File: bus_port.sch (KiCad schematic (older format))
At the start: 0 parts

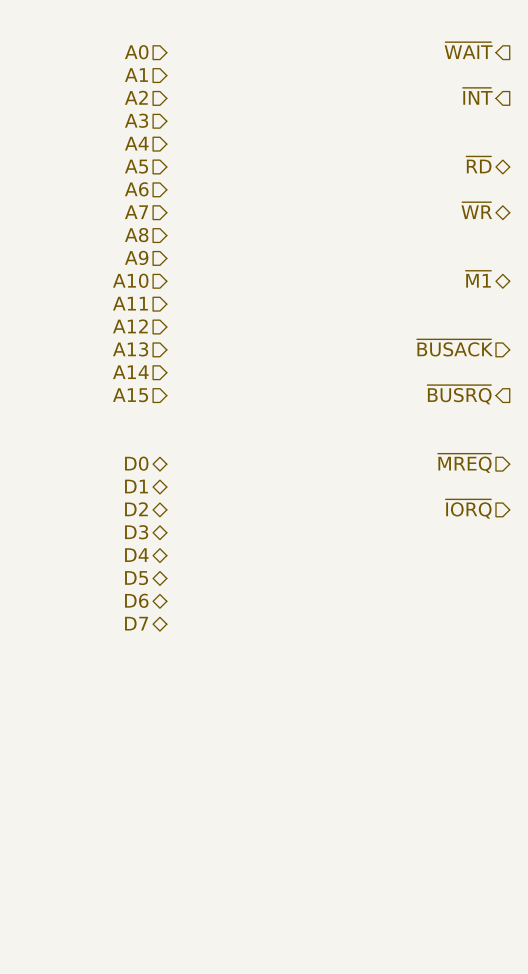
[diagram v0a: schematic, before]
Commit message: More WIP added hierarchical sheets for bus
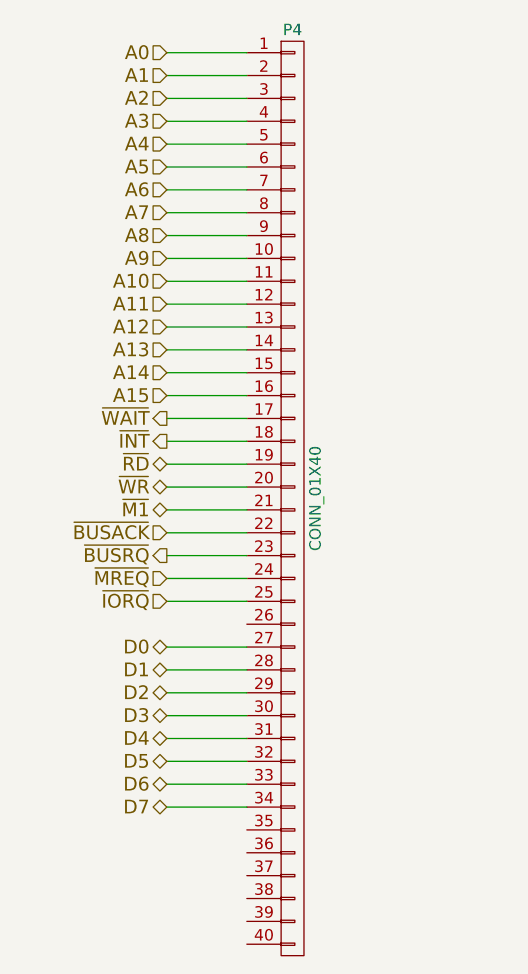
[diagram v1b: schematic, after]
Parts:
- added P1: CONN_01X40, Socket_Strips:Socket_Strip_Straight_1x40, symbol CONN_01X40
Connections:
- net A0: now also P1.1 (P1)
- net A1: now also P1.2 (P2)
- net A10: now also P1.11 (P11)
- net A11: now also P1.12 (P12)
- net A12: now also P1.13 (P13)
- net A13: now also P1.14 (P14)
- net A14: now also P1.15 (P15)
- net A15: now also P1.16 (P16)
- net A2: now also P1.3 (P3)
- net A3: now also P1.4 (P4)
- net A4: now also P1.5 (P5)
- net A5: now also P1.6 (P6)
- net A6: now also P1.7 (P7)
- net A7: now also P1.8 (P8)
- net A8: now also P1.9 (P9)
- net A9: now also P1.10 (P10)
- net D0: now also P1.27 (P27)
- net D1: now also P1.28 (P28)
- net D2: now also P1.29 (P29)
- net D3: now also P1.30 (P30)
- net D4: now also P1.31 (P31)
- net D5: now also P1.32 (P32)
- net D6: now also P1.33 (P33)
- net D7: now also P1.34 (P34)
- net ~BUSACK: now also P1.22 (P22)
- net ~BUSRQ: now also P1.23 (P23)
- net ~INT: now also P1.18 (P18)
- net ~IORQ: now also P1.25 (P25)
- net ~M1: now also P1.21 (P21)
- net ~MREQ: now also P1.24 (P24)
- net ~RD: now also P1.19 (P19)
- net ~WAIT: now also P1.17 (P17)
- net ~WR: now also P1.20 (P20)
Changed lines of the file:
@@
 $Descr A4 11693 8268
 encoding utf-8
-Sheet 4 4
+Sheet 7 7
 Title ""
 Date ""
@@
 Text HLabel 1500 3000 0    60   Input ~ 0
 A15
+Text HLabel 1500 4100 0    60   3State ~ 0
+D0
+Text HLabel 1500 4200 0    60   3State ~ 0
+D1
+Text HLabel 1500 4300 0    60   3State ~ 0
+D2
+Text HLabel 1500 4400 0    60   3State ~ 0
+D3
+Text HLabel 1500 4500 0    60   3State ~ 0
+D4
+Text HLabel 1500 4600 0    60   3State ~ 0
+D5
+Text HLabel 1500 4700 0    60   3State ~ 0
+D6
+Text HLabel 1500 4800 0    60   3State ~ 0
+D7
+Text HLabel 1500 3100 0    60   Output ~ 0
+~WAIT
+Text HLabel 1500 3200 0    60   Output ~ 0
+~INT
 Text HLabel 1500 3300 0    60   3State ~ 0
-D0
+~RD
 Text HLabel 1500 3400 0    60   3State ~ 0
-D1
+~WR
 Text HLabel 1500 3500 0    60   3State ~ 0
-D2
-Text HLabel 1500 3600 0    60   3State ~ 0
-D3
-Text HLabel 1500 3700 0    60   3State ~ 0
-D4
-Text HLabel 1500 3800 0    60   3State ~ 0
-D5
-Text HLabel 1500 3900 0    60   3State ~ 0
-D6
-Text HLabel 1500 4000 0    60   3State ~ 0
-D7
-Text HLabel 3000 1500 0    60   Output ~ 0
-~WAIT
-Text HLabel 3000 1700 0    60   Output ~ 0
-~INT
-Text HLabel 3000 2000 0    60   3State ~ 0
-~RD
-Text HLabel 3000 2200 0    60   3State ~ 0
-~WR
-Text HLabel 3000 2500 0    60   3State ~ 0
 ~M1
-Text HLabel 3000 2800 0    60   Input ~ 0
+Text HLabel 1500 3600 0    60   Input ~ 0
 ~BUSACK
-Text HLabel 3000 3000 0    60   Output ~ 0
+Text HLabel 1500 3700 0    60   Output ~ 0
 ~BUSRQ
-Text HLabel 3000 3300 0    60   Input ~ 0
+Text HLabel 1500 3800 0    60   Input ~ 0
 ~MREQ
-Text HLabel 3000 3500 0    60   Input ~ 0
+Text HLabel 1500 3900 0    60   Input ~ 0
 ~IORQ
+$Comp
+L CONN_01X40 P1
+U 1 1 577CEB68
+P 2050 3450
+AR Path="/577BB11C/577CEB68" Ref="P1"  Part="1"
+AR Path="/577C4BD1/577CEB68" Ref="P2"  Part="1"
+AR Path="/577F17CE/577F1897/577CEB68" Ref="P1"  Part="1"
+AR Path="/577F17CE/577F7EB3/577CEB68" Ref="P2"  Part="1"
+AR Path="/577F17CE/577F8AF5/577CEB68" Ref="P3"  Part="1"
+AR Path="/577F17CE/577F9440/577CEB68" Ref="P4"  Part="1"
+F 0 "P4" H 2050 5500 50  0000 C CNN
+F 1 "CONN_01X40" V 2150 3450 50  0000 C CNN
+F 2 "Socket_Strips:Socket_Strip_Straight_1x40" H 2050 3450 50  0001 C CNN
+F 3 "" H 2050 3450 50  0000 C CNN
+	1    2050 3450
+	1    0    0    -1
+$EndComp
+Wire Wire Line
+	1500 1500 1850 1500
+Wire Wire Line
+	1500 1600 1850 1600
+Wire Wire Line
+	1500 1700 1850 1700
+Wire Wire Line
+	1500 1800 1850 1800
+Wire Wire Line
+	1500 1900 1850 1900
+Wire Wire Line
+	1500 2000 1850 2000
+Wire Wire Line
+	1500 2100 1850 2100
+Wire Wire Line
+	1500 2200 1850 2200
+Wire Wire Line
+	1500 2300 1850 2300
+Wire Wire Line
+	1500 2400 1850 2400
+Wire Wire Line
+	1500 2500 1850 2500
+Wire Wire Line
+	1500 2600 1850 2600
+Wire Wire Line
+	1500 2700 1850 2700
+Wire Wire Line
+	1500 2800 1850 2800
+Wire Wire Line
+	1500 2900 1850 2900
+Wire Wire Line
+	1500 3000 1850 3000
+Wire Wire Line
+	1500 4100 1850 4100
+Wire Wire Line
+	1500 4200 1850 4200
+Wire Wire Line
+	1500 4300 1850 4300
+Wire Wire Line
+	1500 4400 1850 4400
+Wire Wire Line
+	1500 4500 1850 4500
+Wire Wire Line
+	1500 4600 1850 4600
+Wire Wire Line
+	1500 4700 1850 4700
+Wire Wire Line
+	1500 4800 1850 4800
+Wire Wire Line
+	1500 3100 1850 3100
+Wire Wire Line
+	1500 3200 1850 3200
+Wire Wire Line
+	1500 3300 1850 3300
+Wire Wire Line
+	1500 3400 1850 3400
+Wire Wire Line
+	1500 3500 1850 3500
+Wire Wire Line
+	1500 3600 1850 3600
+Wire Wire Line
+	1500 3700 1850 3700
+Wire Wire Line
+	1500 3800 1850 3800
+Wire Wire Line
+	1500 3900 1850 3900
 $EndSCHEMATC

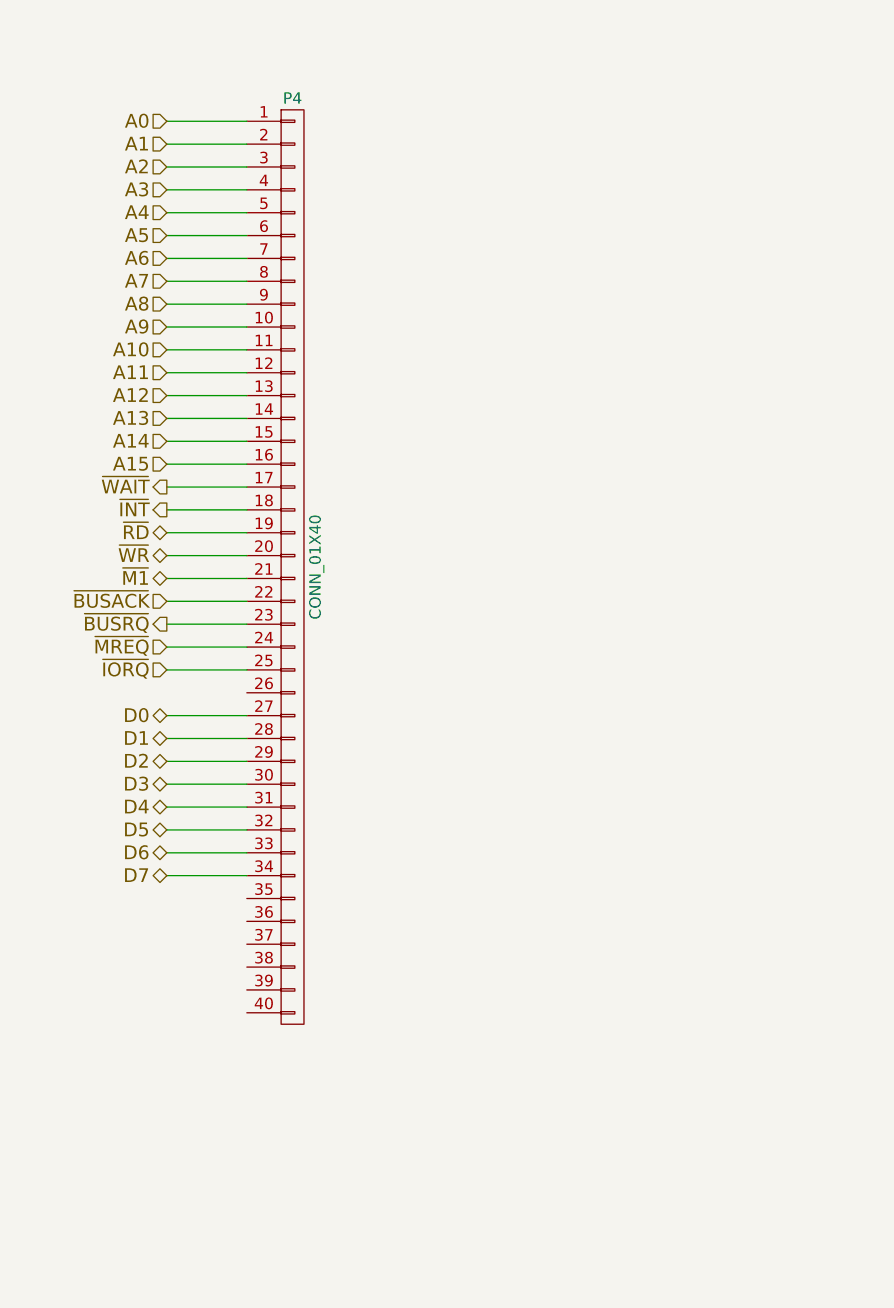
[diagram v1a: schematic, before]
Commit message: Added seperate power pin slots to stop inserting cards backwards
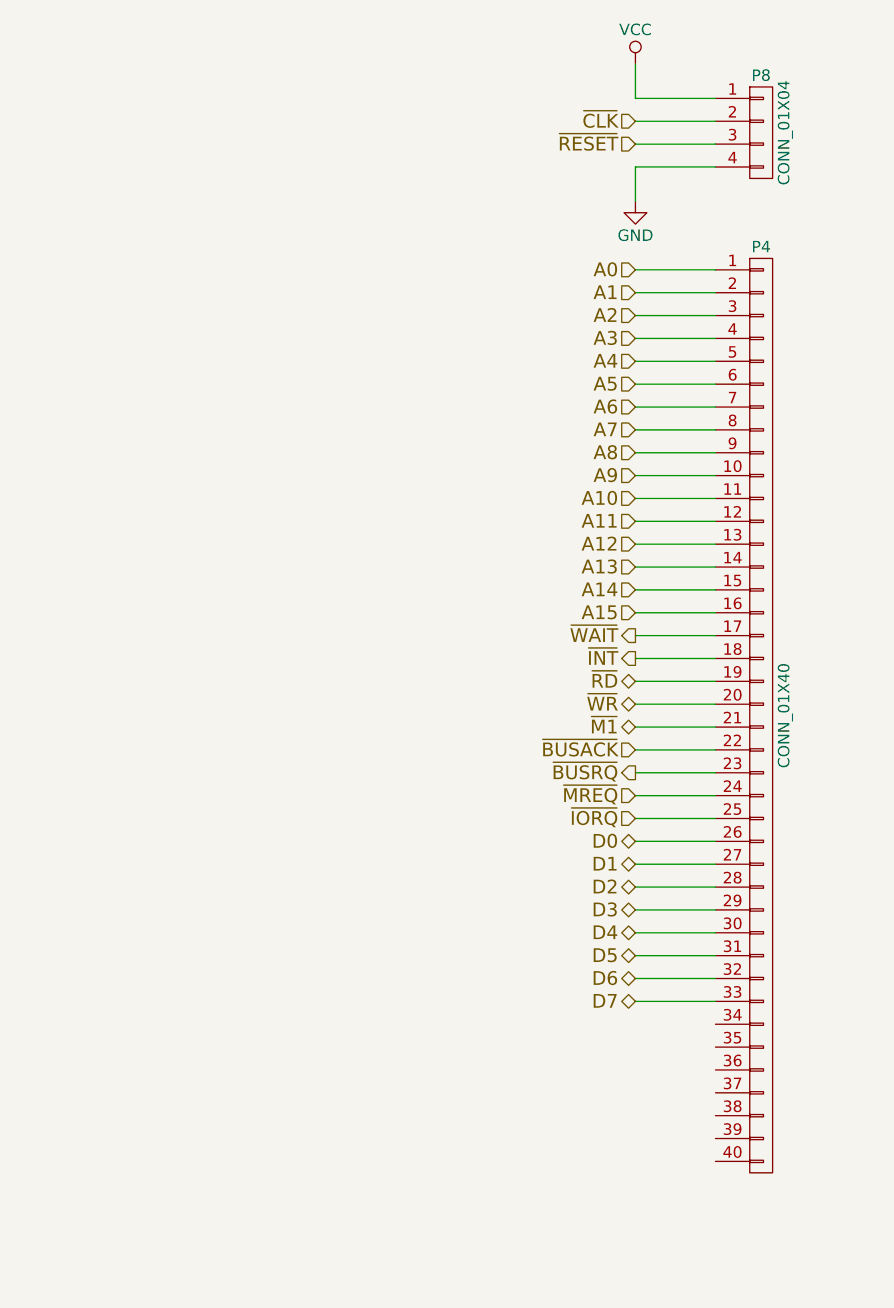
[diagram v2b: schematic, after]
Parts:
- added P5: CONN_01X04, symbol CONN_01X04
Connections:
- net D0: now also P1.26 (P26); no longer P1.27 (P27)
- net D1: now also P1.27 (P27); no longer P1.28 (P28)
- net D2: now also P1.28 (P28); no longer P1.29 (P29)
- net D3: now also P1.29 (P29); no longer P1.30 (P30)
- net D4: now also P1.30 (P30); no longer P1.31 (P31)
- net D5: now also P1.31 (P31); no longer P1.32 (P32)
- net D6: now also P1.32 (P32); no longer P1.33 (P33)
- net D7: now also P1.33 (P33); no longer P1.34 (P34)
- new net GND: P5.4 (P4)
- new net VCC: P5.1 (P1)
- new net ~CLK: P5.2 (P2)
- new net ~RESET: P5.3 (P3)
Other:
- moved on the sheet: P4
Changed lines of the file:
@@
 $Descr A4 11693 8268
 encoding utf-8
-Sheet 7 7
+Sheet 4 7
 Title ""
 Date ""
@@
 Comment4 ""
 $EndDescr
-Text HLabel 1500 1500 0    60   Input ~ 0
+Text HLabel 3550 2150 0    60   Input ~ 0
 A0
-Text HLabel 1500 1600 0    60   Input ~ 0
+Text HLabel 3550 2250 0    60   Input ~ 0
 A1
-Text HLabel 1500 1700 0    60   Input ~ 0
+Text HLabel 3550 2350 0    60   Input ~ 0
 A2
-Text HLabel 1500 1800 0    60   Input ~ 0
+Text HLabel 3550 2450 0    60   Input ~ 0
 A3
-Text HLabel 1500 1900 0    60   Input ~ 0
+Text HLabel 3550 2550 0    60   Input ~ 0
 A4
-Text HLabel 1500 2000 0    60   Input ~ 0
+Text HLabel 3550 2650 0    60   Input ~ 0
 A5
-Text HLabel 1500 2100 0    60   Input ~ 0
+Text HLabel 3550 2750 0    60   Input ~ 0
 A6
-Text HLabel 1500 2200 0    60   Input ~ 0
+Text HLabel 3550 2850 0    60   Input ~ 0
 A7
-Text HLabel 1500 2300 0    60   Input ~ 0
+Text HLabel 3550 2950 0    60   Input ~ 0
 A8
-Text HLabel 1500 2400 0    60   Input ~ 0
+Text HLabel 3550 3050 0    60   Input ~ 0
 A9
-Text HLabel 1500 2500 0    60   Input ~ 0
+Text HLabel 3550 3150 0    60   Input ~ 0
 A10
-Text HLabel 1500 2600 0    60   Input ~ 0
+Text HLabel 3550 3250 0    60   Input ~ 0
 A11
-Text HLabel 1500 2700 0    60   Input ~ 0
+Text HLabel 3550 3350 0    60   Input ~ 0
 A12
-Text HLabel 1500 2800 0    60   Input ~ 0
+Text HLabel 3550 3450 0    60   Input ~ 0
 A13
-Text HLabel 1500 2900 0    60   Input ~ 0
+Text HLabel 3550 3550 0    60   Input ~ 0
 A14
-Text HLabel 1500 3000 0    60   Input ~ 0
+Text HLabel 3550 3650 0    60   Input ~ 0
 A15
-Text HLabel 1500 4100 0    60   3State ~ 0
+Text HLabel 3550 4650 0    60   3State ~ 0
 D0
-Text HLabel 1500 4200 0    60   3State ~ 0
+Text HLabel 3550 4750 0    60   3State ~ 0
 D1
-Text HLabel 1500 4300 0    60   3State ~ 0
+Text HLabel 3550 4850 0    60   3State ~ 0
 D2
-Text HLabel 1500 4400 0    60   3State ~ 0
+Text HLabel 3550 4950 0    60   3State ~ 0
 D3
-Text HLabel 1500 4500 0    60   3State ~ 0
+Text HLabel 3550 5050 0    60   3State ~ 0
 D4
-Text HLabel 1500 4600 0    60   3State ~ 0
+Text HLabel 3550 5150 0    60   3State ~ 0
 D5
-Text HLabel 1500 4700 0    60   3State ~ 0
+Text HLabel 3550 5250 0    60   3State ~ 0
 D6
-Text HLabel 1500 4800 0    60   3State ~ 0
+Text HLabel 3550 5350 0    60   3State ~ 0
 D7
-Text HLabel 1500 3100 0    60   Output ~ 0
+Text HLabel 3550 3750 0    60   Output ~ 0
 ~WAIT
-Text HLabel 1500 3200 0    60   Output ~ 0
+Text HLabel 3550 3850 0    60   Output ~ 0
 ~INT
-Text HLabel 1500 3300 0    60   3State ~ 0
+Text HLabel 3550 3950 0    60   3State ~ 0
 ~RD
-Text HLabel 1500 3400 0    60   3State ~ 0
+Text HLabel 3550 4050 0    60   3State ~ 0
 ~WR
-Text HLabel 1500 3500 0    60   3State ~ 0
+Text HLabel 3550 4150 0    60   3State ~ 0
 ~M1
-Text HLabel 1500 3600 0    60   Input ~ 0
+Text HLabel 3550 4250 0    60   Input ~ 0
 ~BUSACK
-Text HLabel 1500 3700 0    60   Output ~ 0
+Text HLabel 3550 4350 0    60   Output ~ 0
 ~BUSRQ
-Text HLabel 1500 3800 0    60   Input ~ 0
+Text HLabel 3550 4450 0    60   Input ~ 0
 ~MREQ
-Text HLabel 1500 3900 0    60   Input ~ 0
+Text HLabel 3550 4550 0    60   Input ~ 0
 ~IORQ
 $Comp
 L CONN_01X40 P1
 U 1 1 577CEB68
-P 2050 3450
+P 4100 4100
 AR Path="/577BB11C/577CEB68" Ref="P1"  Part="1"
 AR Path="/577C4BD1/577CEB68" Ref="P2"  Part="1"
@@
 AR Path="/577F17CE/577F8AF5/577CEB68" Ref="P3"  Part="1"
 AR Path="/577F17CE/577F9440/577CEB68" Ref="P4"  Part="1"
-F 0 "P4" H 2050 5500 50  0000 C CNN
-F 1 "CONN_01X40" V 2150 3450 50  0000 C CNN
-F 2 "Socket_Strips:Socket_Strip_Straight_1x40" H 2050 3450 50  0001 C CNN
-F 3 "" H 2050 3450 50  0000 C CNN
-	1    2050 3450
-	1    0    0    -1
-$EndComp
-Wire Wire Line
-	1500 1500 1850 1500
-Wire Wire Line
-	1500 1600 1850 1600
-Wire Wire Line
-	1500 1700 1850 1700
-Wire Wire Line
-	1500 1800 1850 1800
-Wire Wire Line
-	1500 1900 1850 1900
-Wire Wire Line
-	1500 2000 1850 2000
-Wire Wire Line
-	1500 2100 1850 2100
-Wire Wire Line
-	1500 2200 1850 2200
-Wire Wire Line
-	1500 2300 1850 2300
-Wire Wire Line
-	1500 2400 1850 2400
-Wire Wire Line
-	1500 2500 1850 2500
-Wire Wire Line
-	1500 2600 1850 2600
-Wire Wire Line
-	1500 2700 1850 2700
-Wire Wire Line
-	1500 2800 1850 2800
-Wire Wire Line
-	1500 2900 1850 2900
-Wire Wire Line
-	1500 3000 1850 3000
-Wire Wire Line
-	1500 4100 1850 4100
-Wire Wire Line
-	1500 4200 1850 4200
-Wire Wire Line
-	1500 4300 1850 4300
-Wire Wire Line
-	1500 4400 1850 4400
-Wire Wire Line
-	1500 4500 1850 4500
-Wire Wire Line
-	1500 4600 1850 4600
-Wire Wire Line
-	1500 4700 1850 4700
-Wire Wire Line
-	1500 4800 1850 4800
-Wire Wire Line
-	1500 3100 1850 3100
-Wire Wire Line
-	1500 3200 1850 3200
-Wire Wire Line
-	1500 3300 1850 3300
-Wire Wire Line
-	1500 3400 1850 3400
-Wire Wire Line
-	1500 3500 1850 3500
-Wire Wire Line
-	1500 3600 1850 3600
-Wire Wire Line
-	1500 3700 1850 3700
-Wire Wire Line
-	1500 3800 1850 3800
-Wire Wire Line
-	1500 3900 1850 3900
+F 0 "P4" H 4100 6150 50  0000 C CNN
+F 1 "CONN_01X40" V 4200 4100 50  0000 C CNN
+F 2 "Socket_Strips:Socket_Strip_Straight_1x40" H 4100 4100 50  0001 C CNN
+F 3 "" H 4100 4100 50  0000 C CNN
+	1    4100 4100
+	1    0    0    -1
+$EndComp
+Wire Wire Line
+	3550 2150 3900 2150
+Wire Wire Line
+	3550 2250 3900 2250
+Wire Wire Line
+	3550 2350 3900 2350
+Wire Wire Line
+	3550 2450 3900 2450
+Wire Wire Line
+	3550 2550 3900 2550
+Wire Wire Line
+	3550 2650 3900 2650
+Wire Wire Line
+	3550 2750 3900 2750
+Wire Wire Line
+	3550 2850 3900 2850
+Wire Wire Line
+	3550 2950 3900 2950
+Wire Wire Line
+	3550 3050 3900 3050
+Wire Wire Line
+	3550 3150 3900 3150
+Wire Wire Line
+	3550 3250 3900 3250
+Wire Wire Line
+	3550 3350 3900 3350
+Wire Wire Line
+	3550 3450 3900 3450
+Wire Wire Line
+	3550 3550 3900 3550
+Wire Wire Line
+	3550 3650 3900 3650
+Wire Wire Line
+	3550 4650 3900 4650
+Wire Wire Line
+	3550 4750 3900 4750
+Wire Wire Line
+	3550 4850 3900 4850
+Wire Wire Line
+	3550 4950 3900 4950
+Wire Wire Line
+	3550 5050 3900 5050
+Wire Wire Line
+	3550 5150 3900 5150
+Wire Wire Line
+	3550 5250 3900 5250
+Wire Wire Line
+	3550 5350 3900 5350
+Wire Wire Line
+	3550 3750 3900 3750
+Wire Wire Line
+	3550 3850 3900 3850
+Wire Wire Line
+	3550 3950 3900 3950
+Wire Wire Line
+	3550 4050 3900 4050
+Wire Wire Line
+	3550 4150 3900 4150
+Wire Wire Line
+	3550 4250 3900 4250
+Wire Wire Line
+	3550 4350 3900 4350
+Wire Wire Line
+	3550 4450 3900 4450
+Wire Wire Line
+	3550 4550 3900 4550
+Text HLabel 3550 1500 0    60   Input ~ 0
+~CLK
+$Comp
+L CONN_01X04 P5
+U 1 1 578144F7
+P 4100 1550
+AR Path="/577F17CE/577F1897/578144F7" Ref="P5"  Part="1"
+AR Path="/577F17CE/577F7EB3/578144F7" Ref="P6"  Part="1"
+AR Path="/577F17CE/577F8AF5/578144F7" Ref="P7"  Part="1"
+AR Path="/577F17CE/577F9440/578144F7" Ref="P8"  Part="1"
+F 0 "P8" H 4100 1800 50  0000 C CNN
+F 1 "CONN_01X04" V 4200 1550 50  0000 C CNN
+F 2 "" H 4100 1550 50  0000 C CNN
+F 3 "" H 4100 1550 50  0000 C CNN
+	1    4100 1550
+	1    0    0    -1
+$EndComp
+Wire Wire Line
+	3900 1400 3550 1400
+Wire Wire Line
+	3550 1400 3550 1250
+$Comp
+L VCC #PWR017
+U 1 1 5781454A
+P 3550 1250
+AR Path="/577F17CE/577F1897/5781454A" Ref="#PWR017"  Part="1"
+AR Path="/577F17CE/577F7EB3/5781454A" Ref="#PWR019"  Part="1"
+AR Path="/577F17CE/577F8AF5/5781454A" Ref="#PWR021"  Part="1"
+AR Path="/577F17CE/577F9440/5781454A" Ref="#PWR023"  Part="1"
+F 0 "#PWR023" H 3550 1100 50  0001 C CNN
+F 1 "VCC" H 3550 1400 50  0000 C CNN
+F 2 "" H 3550 1250 50  0000 C CNN
+F 3 "" H 3550 1250 50  0000 C CNN
+	1    3550 1250
+	1    0    0    -1
+$EndComp
+Wire Wire Line
+	3900 1700 3550 1700
+Wire Wire Line
+	3550 1700 3550 1850
+$Comp
+L GND #PWR018
+U 1 1 5781458A
+P 3550 1850
+AR Path="/577F17CE/577F1897/5781458A" Ref="#PWR018"  Part="1"
+AR Path="/577F17CE/577F7EB3/5781458A" Ref="#PWR020"  Part="1"
+AR Path="/577F17CE/577F8AF5/5781458A" Ref="#PWR022"  Part="1"
+AR Path="/577F17CE/577F9440/5781458A" Ref="#PWR024"  Part="1"
+F 0 "#PWR024" H 3550 1600 50  0001 C CNN
+F 1 "GND" H 3550 1700 50  0000 C CNN
+F 2 "" H 3550 1850 50  0000 C CNN
+F 3 "" H 3550 1850 50  0000 C CNN
+	1    3550 1850
+	1    0    0    -1
+$EndComp
+Wire Wire Line
+	3550 1500 3900 1500
+Wire Wire Line
+	3900 1600 3550 1600
+Text HLabel 3550 1600 0    60   Input ~ 0
+~RESET
 $EndSCHEMATC
